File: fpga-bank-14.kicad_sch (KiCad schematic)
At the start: 8 parts, among them U1 XC7K410T-2FFG900I

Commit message: Add DDR3L decoupling capacitors
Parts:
- gave numbers to parts that had none: 6
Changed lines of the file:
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@@
   (symbol (lib_id "antmicroShuntsJumpers:NetTie_2") (at 172.72 106.68 0) (unit 1)
     (in_bom yes) (on_board yes) (fields_autoplaced)
-    (property "Reference" "NT?" (id 0) (at 172.72 105.41 0)
+    (property "Reference" "NT11" (id 0) (at 172.72 105.41 0)
       (effects (font (size 1.27 1.27)) hide)
     )
@@
   (symbol (lib_id "antmicroShuntsJumpers:NetTie_2") (at 172.72 93.98 0) (unit 1)
     (in_bom yes) (on_board yes) (fields_autoplaced)
-    (property "Reference" "NT?" (id 0) (at 172.72 92.71 0)
+    (property "Reference" "NT9" (id 0) (at 172.72 92.71 0)
       (effects (font (size 1.27 1.27)) hide)
     )
@@
   (symbol (lib_id "antmicroShuntsJumpers:NetTie_2") (at 172.72 104.14 0) (unit 1)
     (in_bom yes) (on_board yes) (fields_autoplaced)
-    (property "Reference" "NT?" (id 0) (at 172.72 102.87 0)
+    (property "Reference" "NT10" (id 0) (at 172.72 102.87 0)
       (effects (font (size 1.27 1.27)) hide)
     )
@@
   (symbol (lib_id "antmicroShuntsJumpers:NetTie_2") (at 195.58 88.9 0) (unit 1)
     (in_bom yes) (on_board yes) (fields_autoplaced)
-    (property "Reference" "NT?" (id 0) (at 195.58 87.63 0)
+    (property "Reference" "NT14" (id 0) (at 195.58 87.63 0)
       (effects (font (size 1.27 1.27)) hide)
     )
@@
   (symbol (lib_id "antmicroShuntsJumpers:NetTie_2") (at 172.72 109.22 0) (unit 1)
     (in_bom yes) (on_board yes) (fields_autoplaced)
-    (property "Reference" "NT?" (id 0) (at 172.72 107.95 0)
+    (property "Reference" "NT12" (id 0) (at 172.72 107.95 0)
       (effects (font (size 1.27 1.27)) hide)
     )
@@
   (symbol (lib_id "antmicroShuntsJumpers:NetTie_2") (at 195.58 86.36 0) (unit 1)
     (in_bom yes) (on_board yes) (fields_autoplaced)
-    (property "Reference" "NT?" (id 0) (at 195.58 85.09 0)
-      (effects (font (size 1.27 1.27)) hide)
-    )
+    (property "Reference" "NT13" (id 0) (at 195.58 85.09 0)
+      (effects (font (size 1.27 1.27)) hide)
+    )

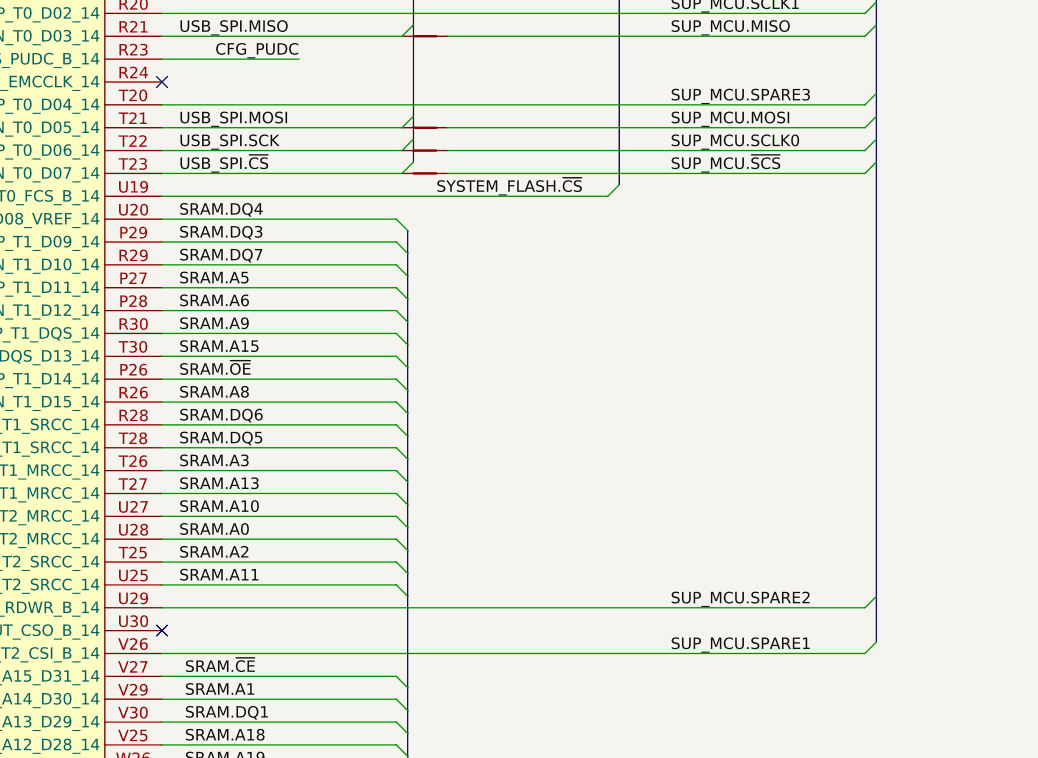
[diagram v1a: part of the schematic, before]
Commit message: Connect MCU CFG_CS signal to system FLASH CS signal
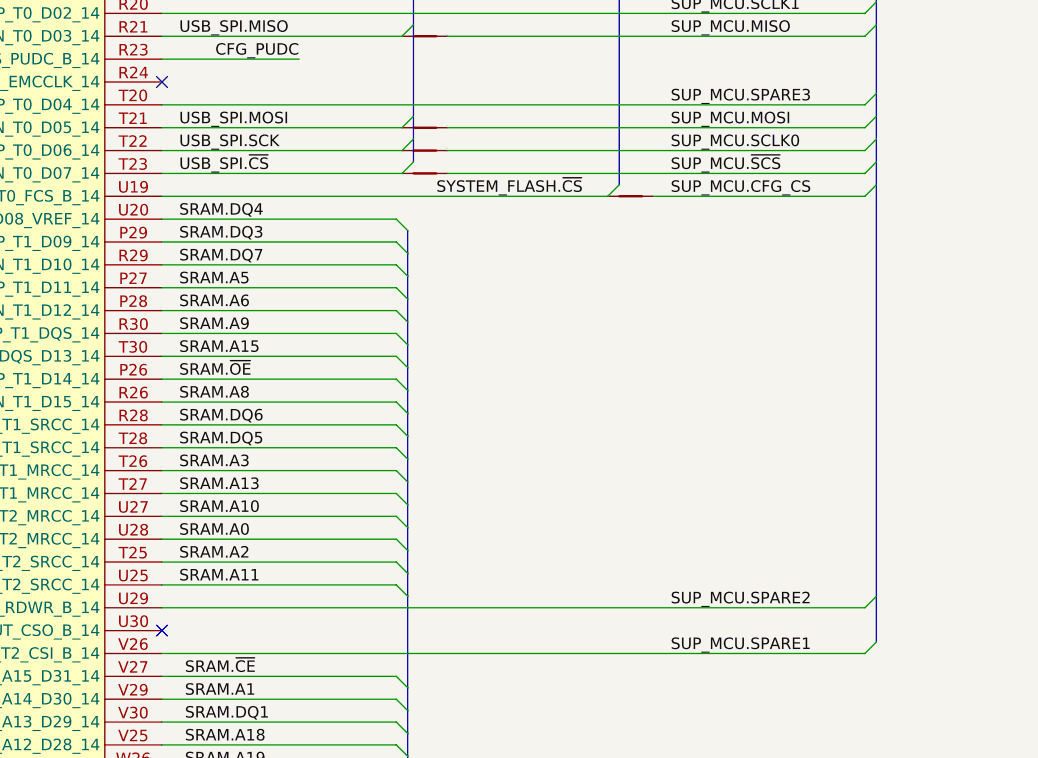
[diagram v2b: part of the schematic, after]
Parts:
- added NT?: NetTie_2, antmicro-footprints:NetTie-2_SMD_Pad0.127mm, symbol antmicroShuntsJumpers:NetTie_2
- renumbered NT11 to NT?, NT9 to NT?, NT10 to NT?, NT14 to NT?, NT12 to NT?, NT13 to NT?
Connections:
- net SYSTEM_FLASH.~{CS}: now also NT?.1
- new net SUP_MCU.CFG_CS: NT?.2
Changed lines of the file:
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@@
+    (stroke (width 0) (type default) (color 0 0 0 0))
+  )
+  (bus_entry (at 222.885 110.49) (size -1.27 1.27)
     (stroke (width 0) (type default) (color 0 0 0 0))
   )
@@
     (stroke (width 0) (type default) (color 0 0 0 0))
   )
-  (wire (pts (xy 193.04 111.76) (xy 143.51 111.76))
-    (stroke (width 0) (type default) (color 0 0 0 0))
-  )
   (bus (pts (xy 222.885 90.17) (xy 222.885 92.71))
     (stroke (width 0) (type default) (color 0 0 0 0))
@@
     (stroke (width 0) (type default) (color 0 0 0 0))
   )
-  (bus (pts (xy 222.885 107.95) (xy 222.885 156.21))
+  (bus (pts (xy 222.885 107.95) (xy 222.885 110.49))
     (stroke (width 0) (type default) (color 0 0 0 0))
   )
@@
     (stroke (width 0) (type default) (color 0 0 0 0))
   )
+  (wire (pts (xy 198.12 111.76) (xy 221.615 111.76))
+    (stroke (width 0) (type default) (color 0 0 0 0))
+  )
   (wire (pts (xy 143.51 187.96) (xy 169.545 187.96))
     (stroke (width 0) (type default) (color 0 0 0 0))
@@
     (stroke (width 0) (type default) (color 0 0 0 0))
   )
+  (wire (pts (xy 143.51 111.76) (xy 193.04 111.76))
+    (stroke (width 0) (type default) (color 0 0 0 0))
+  )
   (wire (pts (xy 143.51 162.56) (xy 221.615 162.56))
     (stroke (width 0) (type default) (color 0 0 0 0))
@@
   )
   (bus (pts (xy 222.885 87.63) (xy 222.885 90.17))
+    (stroke (width 0) (type default) (color 0 0 0 0))
+  )
+  (bus (pts (xy 222.885 110.49) (xy 222.885 156.21))
     (stroke (width 0) (type default) (color 0 0 0 0))
   )
@@
     (effects (font (size 1.27 1.27)) (justify left bottom))
   )
+  (label "SUP_MCU.CFG_CS" (at 200.025 111.76 0)
+    (effects (font (size 1.27 1.27)) (justify left bottom))
+  )
   (label "SUP_MCU.MISO" (at 200.025 93.98 0)
     (effects (font (size 1.27 1.27)) (justify left bottom))
@@
   (symbol (lib_id "antmicroShuntsJumpers:NetTie_2") (at 172.72 106.68 0) (unit 1)
     (in_bom yes) (on_board yes) (fields_autoplaced)
-    (property "Reference" "NT11" (id 0) (at 172.72 105.41 0)
+    (property "Reference" "NT?" (id 0) (at 172.72 105.41 0)
       (effects (font (size 1.27 1.27)) hide)
     )
@@
   (symbol (lib_id "antmicroShuntsJumpers:NetTie_2") (at 172.72 93.98 0) (unit 1)
     (in_bom yes) (on_board yes) (fields_autoplaced)
-    (property "Reference" "NT9" (id 0) (at 172.72 92.71 0)
+    (property "Reference" "NT?" (id 0) (at 172.72 92.71 0)
       (effects (font (size 1.27 1.27)) hide)
     )
@@
   (symbol (lib_id "antmicroShuntsJumpers:NetTie_2") (at 172.72 104.14 0) (unit 1)
     (in_bom yes) (on_board yes) (fields_autoplaced)
-    (property "Reference" "NT10" (id 0) (at 172.72 102.87 0)
+    (property "Reference" "NT?" (id 0) (at 172.72 102.87 0)
       (effects (font (size 1.27 1.27)) hide)
     )
@@
     (pin "2")
   )
+  (symbol (lib_id "antmicroShuntsJumpers:NetTie_2") (at 195.58 111.76 0) (unit 1)
+    (in_bom yes) (on_board yes) (fields_autoplaced)
+    (property "Reference" "NT?" (id 0) (at 195.58 110.49 0)
+      (effects (font (size 1.27 1.27)) hide)
+    )
+    (property "Value" "NetTie_2" (id 1) (at 195.58 113.03 0)
+      (effects (font (size 1.27 1.27)) hide)
+    )
+    (property "Footprint" "antmicro-footprints:NetTie-2_SMD_Pad0.127mm" (id 2) (at 195.58 111.76 0)
+      (effects (font (size 1.27 1.27)) hide)
+    )
+    (property "Datasheet" "~" (id 3) (at 195.58 111.76 0)
+      (effects (font (size 1.27 1.27)) hide)
+    )
+    (pin "1")
+    (pin "2")
+  )
   (symbol (lib_id "antmicroShuntsJumpers:NetTie_2") (at 195.58 88.9 0) (unit 1)
     (in_bom yes) (on_board yes) (fields_autoplaced)
-    (property "Reference" "NT14" (id 0) (at 195.58 87.63 0)
+    (property "Reference" "NT?" (id 0) (at 195.58 87.63 0)
       (effects (font (size 1.27 1.27)) hide)
     )
@@
   (symbol (lib_id "antmicroShuntsJumpers:NetTie_2") (at 172.72 109.22 0) (unit 1)
     (in_bom yes) (on_board yes) (fields_autoplaced)
-    (property "Reference" "NT12" (id 0) (at 172.72 107.95 0)
+    (property "Reference" "NT?" (id 0) (at 172.72 107.95 0)
       (effects (font (size 1.27 1.27)) hide)
     )
@@
   (symbol (lib_id "antmicroShuntsJumpers:NetTie_2") (at 195.58 86.36 0) (unit 1)
     (in_bom yes) (on_board yes) (fields_autoplaced)
-    (property "Reference" "NT13" (id 0) (at 195.58 85.09 0)
-      (effects (font (size 1.27 1.27)) hide)
-    )
+    (property "Reference" "NT?" (id 0) (at 195.58 85.09 0)
+      (effects (font (size 1.27 1.27)) hide)
+    )

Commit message: Fix DDR3L placement
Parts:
- gave numbers to parts that had none: 7
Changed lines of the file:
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@@
   (symbol (lib_id "antmicroShuntsJumpers:NetTie_2") (at 172.72 106.68 0) (unit 1)
     (in_bom yes) (on_board yes) (fields_autoplaced)
-    (property "Reference" "NT?" (id 0) (at 172.72 105.41 0)
+    (property "Reference" "NT11" (id 0) (at 172.72 105.41 0)
       (effects (font (size 1.27 1.27)) hide)
     )
@@
   (symbol (lib_id "antmicroShuntsJumpers:NetTie_2") (at 172.72 93.98 0) (unit 1)
     (in_bom yes) (on_board yes) (fields_autoplaced)
-    (property "Reference" "NT?" (id 0) (at 172.72 92.71 0)
+    (property "Reference" "NT9" (id 0) (at 172.72 92.71 0)
       (effects (font (size 1.27 1.27)) hide)
     )
@@
   (symbol (lib_id "antmicroShuntsJumpers:NetTie_2") (at 172.72 104.14 0) (unit 1)
     (in_bom yes) (on_board yes) (fields_autoplaced)
-    (property "Reference" "NT?" (id 0) (at 172.72 102.87 0)
+    (property "Reference" "NT10" (id 0) (at 172.72 102.87 0)
       (effects (font (size 1.27 1.27)) hide)
     )
@@
   (symbol (lib_id "antmicroShuntsJumpers:NetTie_2") (at 195.58 111.76 0) (unit 1)
     (in_bom yes) (on_board yes) (fields_autoplaced)
-    (property "Reference" "NT?" (id 0) (at 195.58 110.49 0)
+    (property "Reference" "NT20" (id 0) (at 195.58 110.49 0)
       (effects (font (size 1.27 1.27)) hide)
     )
@@
   (symbol (lib_id "antmicroShuntsJumpers:NetTie_2") (at 195.58 88.9 0) (unit 1)
     (in_bom yes) (on_board yes) (fields_autoplaced)
-    (property "Reference" "NT?" (id 0) (at 195.58 87.63 0)
+    (property "Reference" "NT14" (id 0) (at 195.58 87.63 0)
       (effects (font (size 1.27 1.27)) hide)
     )
@@
   (symbol (lib_id "antmicroShuntsJumpers:NetTie_2") (at 172.72 109.22 0) (unit 1)
     (in_bom yes) (on_board yes) (fields_autoplaced)
-    (property "Reference" "NT?" (id 0) (at 172.72 107.95 0)
+    (property "Reference" "NT12" (id 0) (at 172.72 107.95 0)
       (effects (font (size 1.27 1.27)) hide)
     )
@@
   (symbol (lib_id "antmicroShuntsJumpers:NetTie_2") (at 195.58 86.36 0) (unit 1)
     (in_bom yes) (on_board yes) (fields_autoplaced)
-    (property "Reference" "NT?" (id 0) (at 195.58 85.09 0)
-      (effects (font (size 1.27 1.27)) hide)
-    )
+    (property "Reference" "NT13" (id 0) (at 195.58 85.09 0)
+      (effects (font (size 1.27 1.27)) hide)
+    )

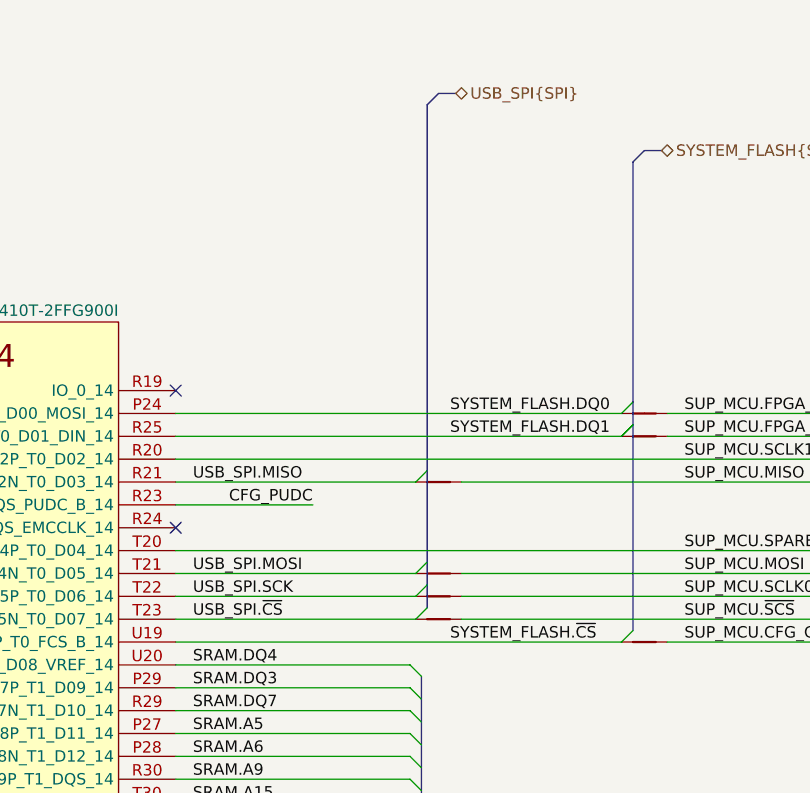
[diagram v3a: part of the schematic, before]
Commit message: Connected DQ2 DQ3 lines of SPI flash to FPGA bank 14
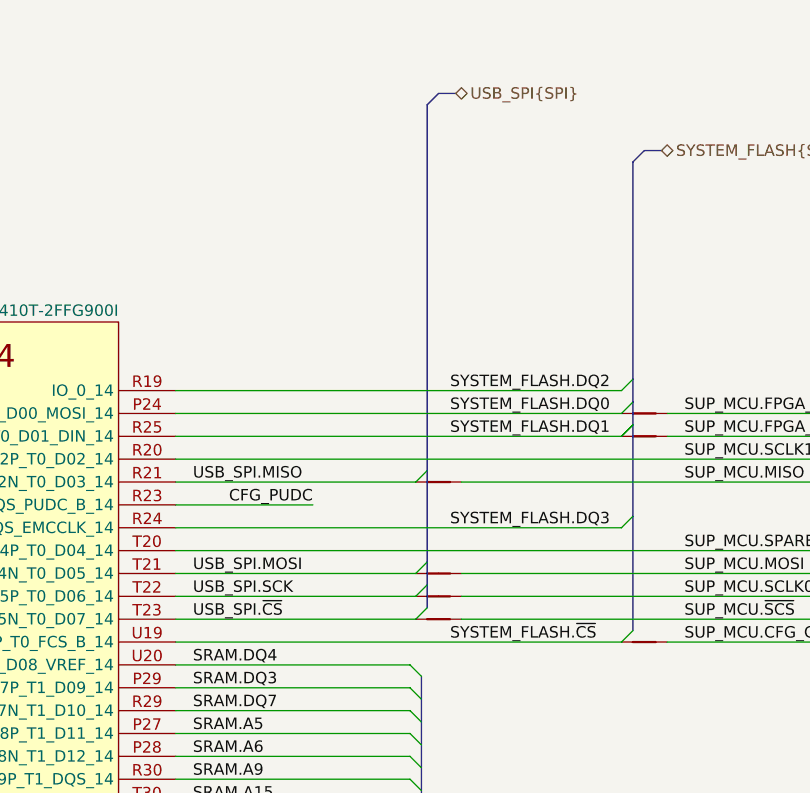
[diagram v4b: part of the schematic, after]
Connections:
- net SYSTEM_FLASH.DQ2: now reaches U1.R19 (IO_0_14)
- net SYSTEM_FLASH.DQ3: now reaches U1.R24 (IO_L3N_T0_DQS_EMCCLK_14)
- no-connect marks 6 -> 4
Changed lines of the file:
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@@
   (no_connect (at 143.51 208.28))
   (no_connect (at 143.51 195.58))
-  (no_connect (at 143.51 83.82))
-  (no_connect (at 143.51 99.06))
   (no_connect (at 143.51 198.12))
   (no_connect (at 143.51 160.02))
@@
     (stroke (width 0) (type default) (color 0 0 0 0))
   )
+  (bus_entry (at 194.31 82.55) (size -1.27 1.27)
+    (stroke (width 0) (type default) (color 0 0 0 0))
+  )
   (bus_entry (at 222.885 102.87) (size -1.27 1.27)
     (stroke (width 0) (type default) (color 0 0 0 0))
@@
     (stroke (width 0) (type default) (color 0 0 0 0))
   )
+  (bus_entry (at 194.31 97.79) (size -1.27 1.27)
+    (stroke (width 0) (type default) (color 0 0 0 0))
+  )
   (bus_entry (at 169.545 170.18) (size 1.27 1.27)
     (stroke (width 0) (type default) (color 0 0 0 0))
@@
     (stroke (width 0) (type default) (color 0 0 0 0))
   )
-  (bus (pts (xy 194.31 58.42) (xy 194.31 85.09))
+  (bus (pts (xy 194.31 58.42) (xy 194.31 82.55))
     (stroke (width 0) (type default) (color 0 0 0 0))
   )
@@
     (stroke (width 0) (type default) (color 0 0 0 0))
   )
-  (bus (pts (xy 194.31 87.63) (xy 194.31 110.49))
+  (bus (pts (xy 194.31 87.63) (xy 194.31 97.79))
     (stroke (width 0) (type default) (color 0 0 0 0))
   )
@@
     (stroke (width 0) (type default) (color 0 0 0 0))
   )
+  (wire (pts (xy 143.51 83.82) (xy 193.04 83.82))
+    (stroke (width 0) (type default) (color 0 0 0 0))
+  )
   (bus (pts (xy 172.085 216.535) (xy 170.815 215.265))
     (stroke (width 0) (type default) (color 0 0 0 0))
@@
     (stroke (width 0) (type default) (color 0 0 0 0))
   )
+  (bus (pts (xy 194.31 82.55) (xy 194.31 85.09))
+    (stroke (width 0) (type default) (color 0 0 0 0))
+  )
   (wire (pts (xy 143.51 144.78) (xy 169.545 144.78))
     (stroke (width 0) (type default) (color 0 0 0 0))
@@
     (stroke (width 0) (type default) (color 0 0 0 0))
   )
+  (bus (pts (xy 194.31 97.79) (xy 194.31 110.49))
+    (stroke (width 0) (type default) (color 0 0 0 0))
+  )
   (bus (pts (xy 170.815 191.77) (xy 170.815 194.31))
     (stroke (width 0) (type default) (color 0 0 0 0))
@@
   )
   (bus (pts (xy 170.815 123.19) (xy 170.815 125.73))
+    (stroke (width 0) (type default) (color 0 0 0 0))
+  )
+  (wire (pts (xy 143.51 99.06) (xy 193.04 99.06))
     (stroke (width 0) (type default) (color 0 0 0 0))
   )
@@
     (effects (font (size 1.27 1.27)) (justify left bottom))
   )
+  (label "SYSTEM_FLASH.DQ3" (at 173.99 99.06 0)
+    (effects (font (size 1.27 1.27)) (justify left bottom))
+  )
   (label "USB_SPI.~{CS}" (at 145.415 109.22 0)
     (effects (font (size 1.27 1.27)) (justify left bottom))
@@
     (effects (font (size 1.27 1.27)) (justify left bottom))
   )
+  (label "SYSTEM_FLASH.DQ2" (at 173.99 83.82 0)
+    (effects (font (size 1.27 1.27)) (justify left bottom))
+  )

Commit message: Loclib
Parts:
- NT10, NT11, NT12, NT13, NT14, NT20, NT9: footprint antmicro-footprints:NetTie-2_SMD_Pad0.127mm -> K410T-devboard-footprints:NetTie-2_SMD_Pad0.127mm; symbol antmicroShuntsJumpers:NetTie_2 -> K410T-devboard:NetTie_2
- R338: footprint antmicro-footprints:0402-res -> K410T-devboard-footprints:0402-res; symbol antmicroResistors0402:R_1k_0402 -> K410T-devboard:R_1k_0402
- U1: footprint antmicro-footprints:xc7k410t-2ffg900I -> K410T-devboard-footprints:xc7k410t-2ffg900I; symbol antmicroMicrocontrollers:XC7K410T-2FFG900I -> K410T-devboard:XC7K410T-2FFG900I

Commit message: Finished implementing all changes from sch review
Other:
- note removed: "TODO: -Check DQ2, DQ3, check PD resistor as in CW310"
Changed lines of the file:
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@@
     )
-  )
-  (text "TODO:\n-Check DQ2, DQ3, check PD resistor as in CW310\n"
-    (at 0.635 4.445 0)
-    (effects (font (size 1.27 1.27)) (justify left bottom))
   )
   (label "SUP_MCU.SPARE3" (at 200.025 101.6 0)
